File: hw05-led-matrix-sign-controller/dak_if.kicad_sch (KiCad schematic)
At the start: 8 parts, among them J201 TE 640456-2, J202 TE 640456-4, J203 2x7 Conn to Dak matrix, U201 74HC595

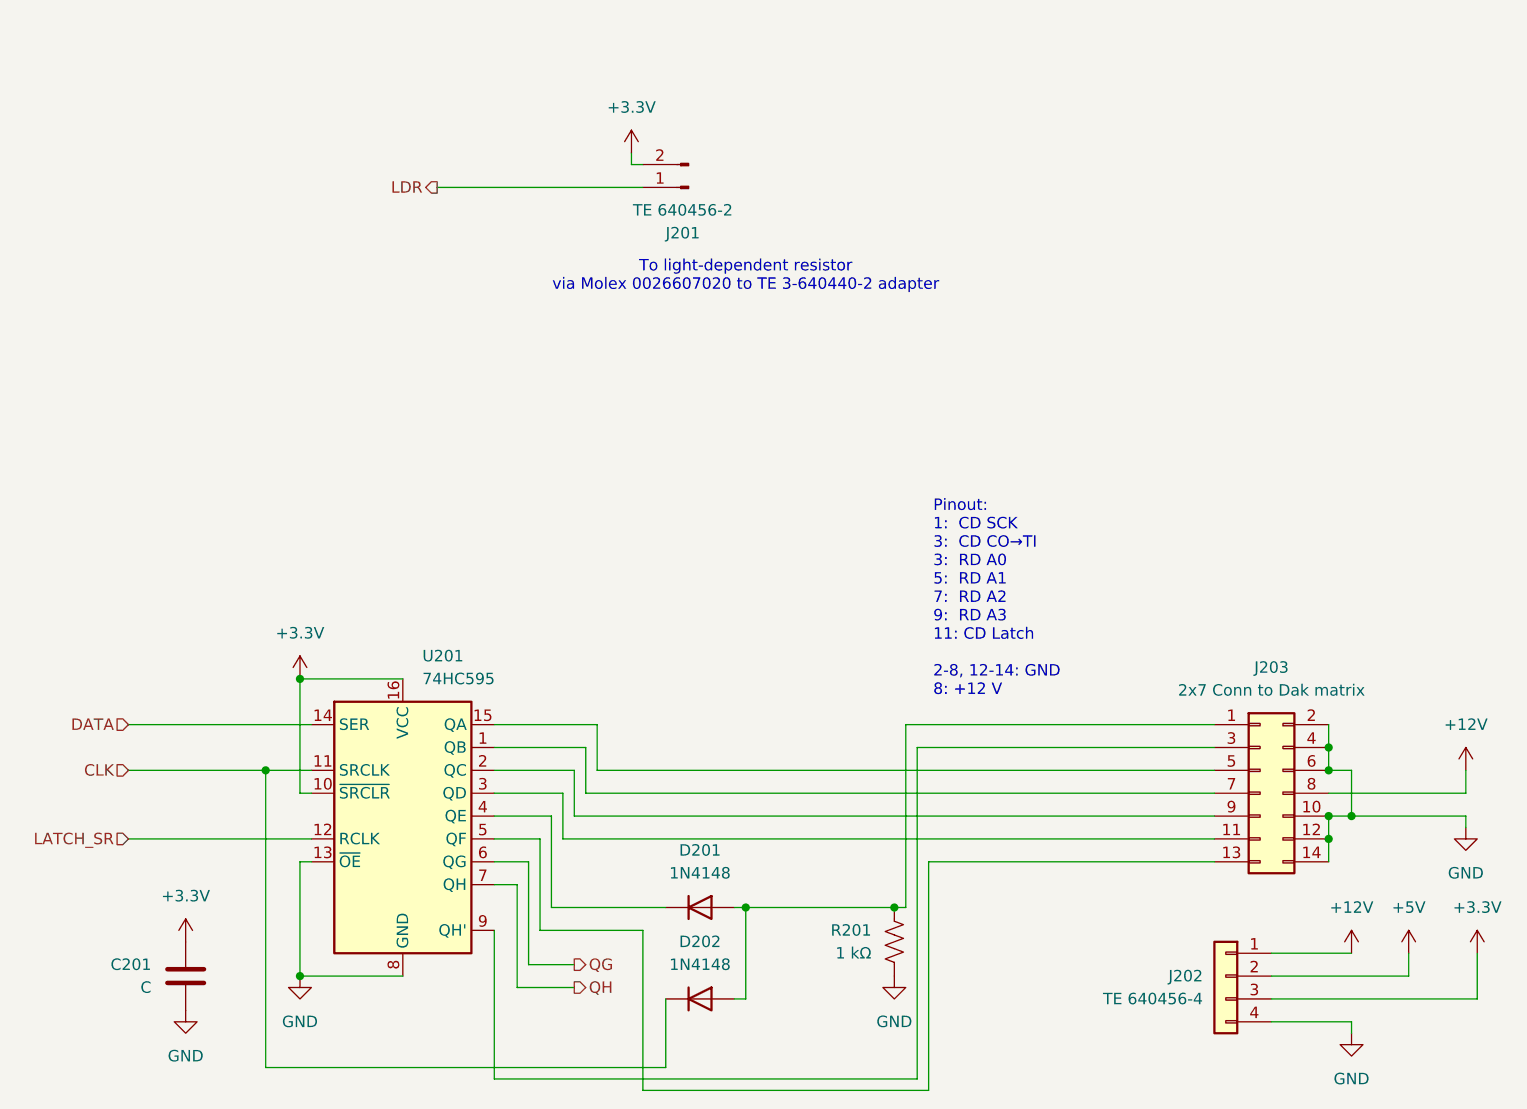
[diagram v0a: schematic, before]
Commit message: Fix pullup
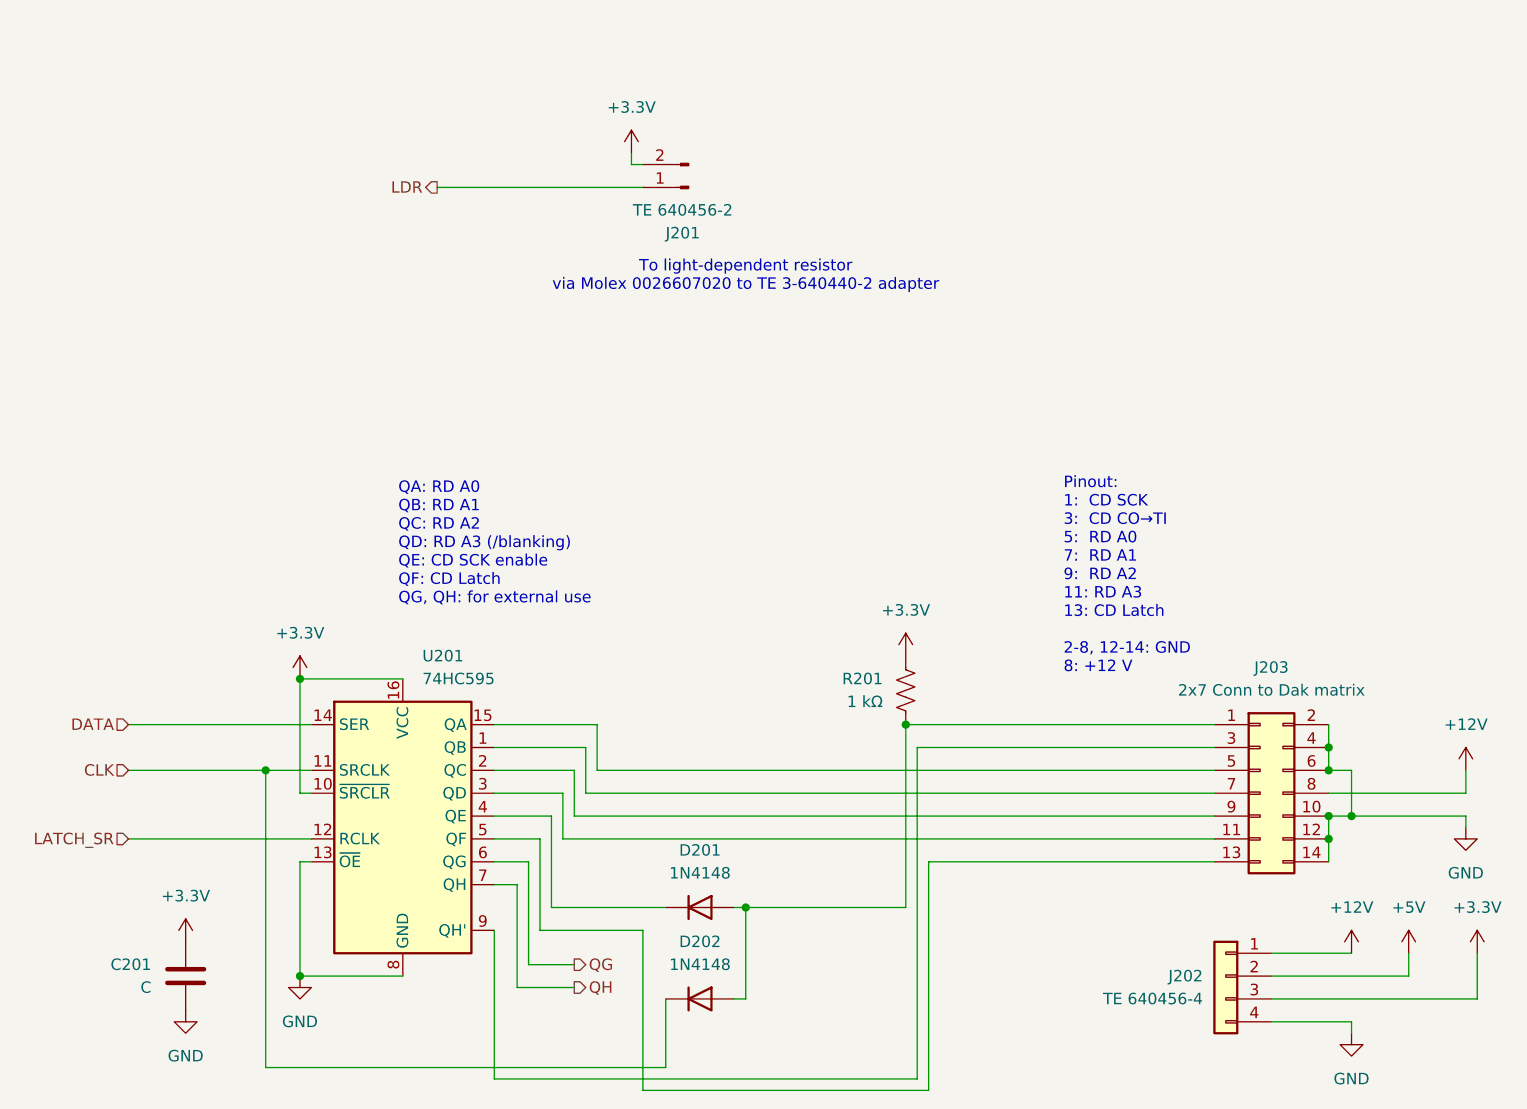
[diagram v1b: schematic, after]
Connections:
- net +3.3V: now also R201.1
- net GND: no longer R201.2
- net at D201.2 (A), D202.2 (A), J203.1 (Pin_1): now also R201.2; no longer R201.1
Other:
- note added: "Pinout: 1: CD SCK 3: CD CO→TI 5: RD A0 7: RD A1 9: RD A2 11: RD A3 13: CD Latch 2-8, 12-14: GND 8: +12 V"
- note added: "QA: RD A0 QB: RD A1 QC: RD A2 QD: RD A3 (/blanking) QE: CD SCK enable QF: CD Latch QG, QH: for external use"
- note removed: "Pinout: 1: CD SCK 3: CD CO→TI 3: RD A0 5: RD A1 7: RD A2 9: RD A3 11: CD Latch 2-8, 12-14: GND 8: +12 V"
- moved on the sheet: R201
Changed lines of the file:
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@@
 	(title_block
 		(title "Daktronics-specific circuitry")
-		(date "2025-08-29")
-		(rev "02")
+		(date "2025-10-08")
+		(rev "03")
 		(company "Bay Area Electric Railroad Association")
 	)
-	(text "Pinout:\n1:  CD SCK\n3:  CD CO→TI\n3:  RD A0\n5:  RD A1\n7:  RD A2\n9:  RD A3\n11: CD Latch\n\n2-8, 12-14: GND\n8: +12 V"
+	(text "Pinout:\n1:  CD SCK\n3:  CD CO→TI\n5:  RD A0\n7:  RD A1\n9:  RD A2\n11: RD A3\n13: CD Latch\n\n2-8, 12-14: GND\n8: +12 V"
 		(exclude_from_sim no)
-		(at 196.088 97.79 0)
+		(at 210.566 95.25 0)
+		(effects
+			(font
+				(size 1.27 1.27)
+			)
+			(justify left)
+		)
+	)
+	(text "QA: RD A0\nQB: RD A1\nQC: RD A2\nQD: RD A3 (/blanking)\nQE: CD SCK enable\nQF: CD Latch\nQG, QH: for external use"
+		(exclude_from_sim no)
+		(at 136.652 91.694 0)
 		(effects
 			(font
@@
 	)
 	(junction
-		(at 191.77 132.08)
-		(diameter 0)
-		(color 0 0 0 0)
-	)
-	(junction
 		(at 125.73 139.7)
 		(diameter 0)
@@
 		(color 0 0 0 0)
 	)
+	(junction
+		(at 193.04 111.76)
+		(diameter 0)
+		(color 0 0 0 0)
+	)
 	(wire
 		(pts
@@
 	(wire
 		(pts
-			(xy 191.77 132.08) (xy 175.26 132.08)
+			(xy 175.26 132.08) (xy 193.04 132.08)
 		)
 		(stroke
@@
 		(pts
 			(xy 156.21 116.84) (xy 147.32 116.84)
-		)
-		(stroke
-			(width 0)
-			(type default)
-		)
-	)
-	(wire
-		(pts
-			(xy 193.04 132.08) (xy 191.77 132.08)
 		)
 		(stroke
@@
 	)
 	(symbol
-		(lib_id "power:GND")
-		(at 191.77 139.7 0)
+		(lib_id "power:+3.3V")
+		(at 193.04 104.14 0)
 		(unit 1)
 		(exclude_from_sim no)
@@
 		(fields_autoplaced yes)
 		(property "Reference" "#PWR0206"
-			(at 191.77 146.05 0)
-			(effects
-				(font
-					(size 1.27 1.27)
-				)
-				(hide yes)
-			)
-		)
-		(property "Value" "GND"
-			(at 191.77 144.78 0)
+			(at 193.04 107.95 0)
+			(effects
+				(font
+					(size 1.27 1.27)
+				)
+				(hide yes)
+			)
+		)
+		(property "Value" "+3.3V"
+			(at 193.04 99.06 0)
 			(effects
 				(font
@@
 		)
 		(property "Footprint" ""
-			(at 191.77 139.7 0)
+			(at 193.04 104.14 0)
 			(effects
 				(font
@@
 		)
 		(property "Datasheet" ""
-			(at 191.77 139.7 0)
-			(effects
-				(font
-					(size 1.27 1.27)
-				)
-				(hide yes)
-			)
-		)
-		(property "Description" "Power symbol creates a global label with name \"GND\" , ground"
-			(at 191.77 139.7 0)
+			(at 193.04 104.14 0)
+			(effects
+				(font
+					(size 1.27 1.27)
+				)
+				(hide yes)
+			)
+		)
+		(property "Description" "Power symbol creates a global label with name \"+3.3V\""
+			(at 193.04 104.14 0)
 			(effects
 				(font
@@
 		)
 		(instances
-			(project ""
+			(project "hw05-led-matrix-sign-controller"
 				(path "/268939db-8332-4e95-b629-4f0847d8eb12/aa11d66a-b9d9-471a-9173-8cee8aff3283"
 					(reference "#PWR0206")
@@
 	(symbol
 		(lib_id "Device:R_US")
-		(at 191.77 135.89 0)
+		(at 193.04 107.95 0)
 		(unit 1)
 		(exclude_from_sim no)
@@
 		(dnp no)
 		(property "Reference" "R201"
-			(at 189.23 134.6199 0)
+			(at 190.5 106.6799 0)
 			(effects
 				(font
@@
 		)
 		(property "Value" "1 kΩ"
-			(at 189.23 137.1599 0)
+			(at 190.5 109.2199 0)
 			(effects
 				(font
@@
 		)
 		(property "Footprint" "Resistor_SMD:R_1206_3216Metric_Pad1.30x1.75mm_HandSolder"
-			(at 192.786 136.144 90)
+			(at 194.056 108.204 90)
 			(effects
 				(font
@@
 		)
 		(property "Datasheet" "~"
-			(at 191.77 135.89 0)
+			(at 193.04 107.95 0)
 			(effects
 				(font
@@
 		)
 		(property "Description" "Resistor, US symbol"
-			(at 191.77 135.89 0)
+			(at 193.04 107.95 0)
 			(effects
 				(font
@@
 		)
 		(instances
-			(project ""
+			(project "hw05-led-matrix-sign-controller"
 				(path "/268939db-8332-4e95-b629-4f0847d8eb12/aa11d66a-b9d9-471a-9173-8cee8aff3283"
 					(reference "R201")

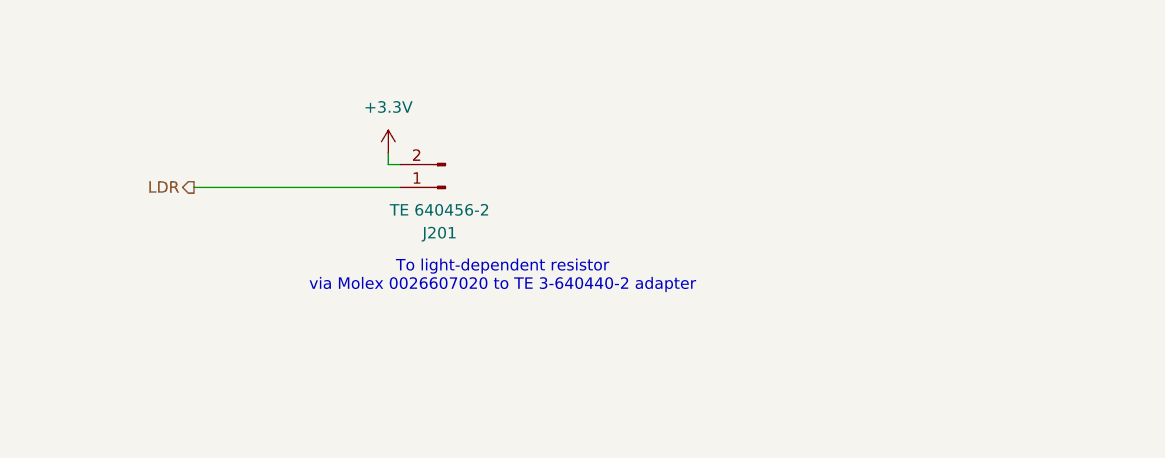
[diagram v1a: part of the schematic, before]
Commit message: Add extra header for direct LDR connection
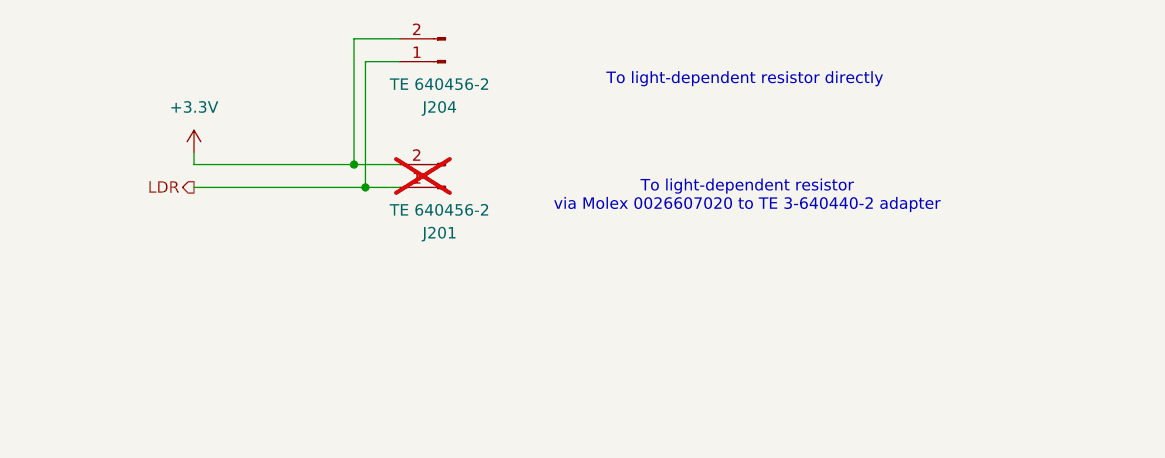
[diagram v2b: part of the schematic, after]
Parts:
- added J204: TE 640456-2, Connector_Molex:Molex_KK-396_A-41791-0002_1x02_P3.96mm_Vertical, symbol Connector:Conn_01x02_Pin
- J201: now not fitted
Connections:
- net +3.3V: now also J204.2 (Pin_2)
- net LDR: now also J204.1 (Pin_1)
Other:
- note added: "To light-dependent resistor directly"
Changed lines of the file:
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@@
 	(text "To light-dependent resistor\nvia Molex 0026607020 to TE 3-640440-2 adapter"
 		(exclude_from_sim no)
-		(at 175.26 61.976 0)
+		(at 202.438 53.086 0)
+		(effects
+			(font
+				(size 1.27 1.27)
+			)
+		)
+	)
+	(text "To light-dependent resistor directly"
+		(exclude_from_sim no)
+		(at 202.184 40.132 0)
 		(effects
 			(font
@@
 	)
 	(junction
+		(at 160.02 52.07)
+		(diameter 0)
+		(color 0 0 0 0)
+	)
+	(junction
 		(at 121.92 116.84)
 		(diameter 0)
@@
 	)
 	(junction
+		(at 158.75 49.53)
+		(diameter 0)
+		(color 0 0 0 0)
+	)
+	(junction
 		(at 193.04 111.76)
 		(diameter 0)
@@
 	(wire
 		(pts
+			(xy 163.83 38.1) (xy 160.02 38.1)
+		)
+		(stroke
+			(width 0)
+			(type default)
+		)
+	)
+	(wire
+		(pts
 			(xy 158.75 116.84) (xy 158.75 111.76)
 		)
@@
 	(wire
 		(pts
+			(xy 160.02 38.1) (xy 160.02 52.07)
+		)
+		(stroke
+			(width 0)
+			(type default)
+		)
+	)
+	(wire
+		(pts
 			(xy 106.68 111.76) (xy 127 111.76)
 		)
@@
 	(wire
 		(pts
+			(xy 160.02 52.07) (xy 163.83 52.07)
+		)
+		(stroke
+			(width 0)
+			(type default)
+		)
+	)
+	(wire
+		(pts
 			(xy 166.37 142.24) (xy 166.37 149.86)
 		)
@@
 	(wire
 		(pts
+			(xy 158.75 49.53) (xy 158.75 35.56)
+		)
+		(stroke
+			(width 0)
+			(type default)
+		)
+	)
+	(wire
+		(pts
 			(xy 166.37 149.86) (xy 121.92 149.86)
 		)
@@
 	(wire
 		(pts
+			(xy 158.75 35.56) (xy 163.83 35.56)
+		)
+		(stroke
+			(width 0)
+			(type default)
+		)
+	)
+	(wire
+		(pts
 			(xy 193.04 111.76) (xy 227.33 111.76)
 		)
@@
 	(wire
 		(pts
-			(xy 162.56 49.53) (xy 163.83 49.53)
+			(xy 140.97 49.53) (xy 158.75 49.53)
 		)
 		(stroke
@@
 	(wire
 		(pts
+			(xy 158.75 49.53) (xy 163.83 49.53)
+		)
+		(stroke
+			(width 0)
+			(type default)
+		)
+	)
+	(wire
+		(pts
 			(xy 153.67 121.92) (xy 153.67 132.08)
 		)
@@
 	(wire
 		(pts
-			(xy 140.97 52.07) (xy 163.83 52.07)
+			(xy 140.97 52.07) (xy 160.02 52.07)
 		)
 		(stroke
@@
 	(wire
 		(pts
-			(xy 162.56 48.26) (xy 162.56 49.53)
+			(xy 140.97 48.26) (xy 140.97 49.53)
 		)
 		(stroke
@@
 	(symbol
 		(lib_id "power:+3.3V")
-		(at 162.56 48.26 0)
+		(at 140.97 48.26 0)
 		(unit 1)
 		(exclude_from_sim no)
@@
 		(fields_autoplaced yes)
 		(property "Reference" "#PWR0205"
-			(at 162.56 52.07 0)
+			(at 140.97 52.07 0)
 			(effects
 				(font
@@
 		)
 		(property "Value" "+3.3V"
-			(at 162.56 43.18 0)
+			(at 140.97 43.18 0)
 			(effects
 				(font
@@
 		)
 		(property "Footprint" ""
-			(at 162.56 48.26 0)
+			(at 140.97 48.26 0)
 			(effects
 				(font
@@
 		)
 		(property "Datasheet" ""
-			(at 162.56 48.26 0)
+			(at 140.97 48.26 0)
 			(effects
 				(font
@@
 		)
 		(property "Description" "Power symbol creates a global label with name \"+3.3V\""
-			(at 162.56 48.26 0)
+			(at 140.97 48.26 0)
 			(effects
 				(font
@@
 	)
 	(symbol
+		(lib_id "Connector:Conn_01x02_Pin")
+		(at 168.91 38.1 180)
+		(unit 1)
+		(exclude_from_sim no)
+		(in_bom yes)
+		(on_board yes)
+		(dnp no)
+		(property "Reference" "J204"
+			(at 168.275 43.18 0)
+			(effects
+				(font
+					(size 1.27 1.27)
+				)
+			)
+		)
+		(property "Value" "TE 640456-2"
+			(at 168.275 40.64 0)
+			(effects
+				(font
+					(size 1.27 1.27)
+				)
+			)
+		)
+		(property "Footprint" "Connector_Molex:Molex_KK-396_A-41791-0002_1x02_P3.96mm_Vertical"
+			(at 168.91 38.1 0)
+			(effects
+				(font
+					(size 1.27 1.27)
+				)
+				(hide yes)
+			)
+		)
+		(property "Datasheet" "~"
+			(at 168.91 38.1 0)
+			(effects
+				(font
+					(size 1.27 1.27)
+				)
+				(hide yes)
+			)
+		)
+		(property "Description" "Generic connector, single row, 01x02, script generated"
+			(at 168.91 38.1 0)
+			(effects
+				(font
+					(size 1.27 1.27)
+				)
+				(hide yes)
+			)
+		)
+		(pin "1"
+		)
+		(pin "2"
+		)
+		(instances
+			(project "hw05-led-matrix-sign-controller"
+				(path "/268939db-8332-4e95-b629-4f0847d8eb12/aa11d66a-b9d9-471a-9173-8cee8aff3283"
+					(reference "J204")
+					(unit 1)
+				)
+			)
+		)
+	)
+	(symbol
 		(lib_id "power:GND")
 		(at 125.73 139.7 0)
@@
 		(in_bom yes)
 		(on_board yes)
-		(dnp no)
+		(dnp yes)
 		(property "Reference" "J201"
 			(at 168.275 57.15 0)
